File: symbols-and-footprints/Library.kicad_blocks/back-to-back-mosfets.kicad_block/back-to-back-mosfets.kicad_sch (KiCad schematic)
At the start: 6 parts

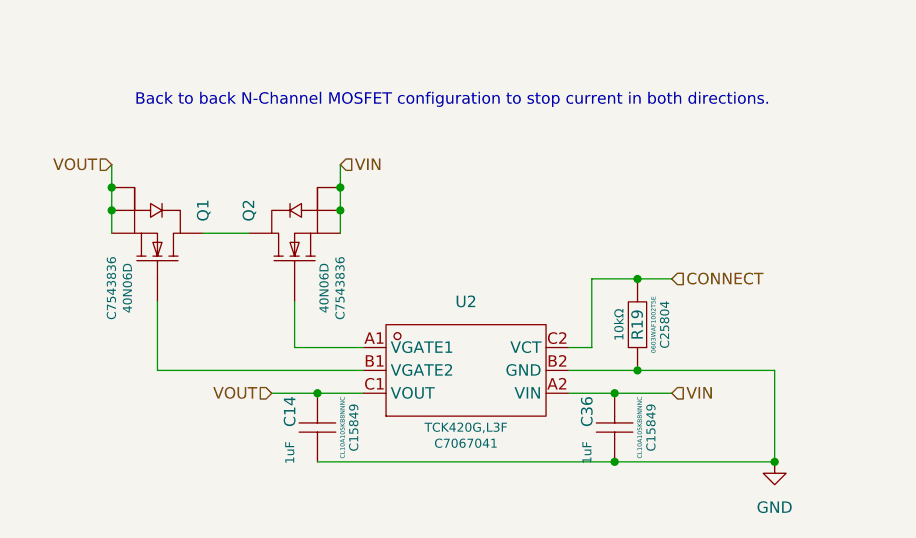
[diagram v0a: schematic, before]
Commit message: Almost complete new master circuit schematic.
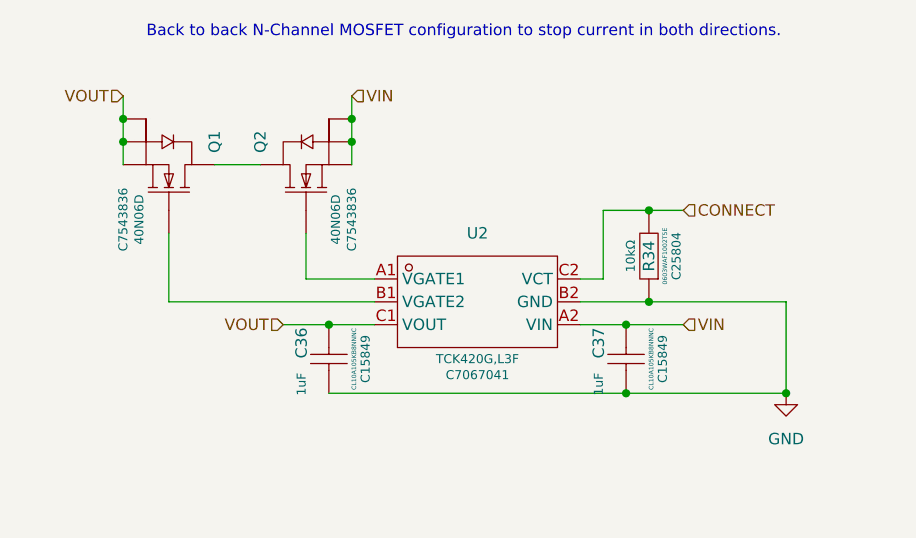
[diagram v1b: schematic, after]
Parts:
- removed C14: 1uF, Library:C0603, symbol Library:CL10A105KB8NNNC Capacitor 1uF
- removed R19: 10kΩ, Library:R0603, symbol Library:0603WAF1002T5E Resistor 10kΩ
- added C37: 1uF, Library:C0603, symbol Library:CL10A105KB8NNNC Capacitor 1uF
- added R34: 10kΩ, Library:R0603, symbol Library:0603WAF1002T5E Resistor 10kΩ
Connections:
- net CONNECT: now also R34.2
- net GND: now also C37.1, R34.1
- net VIN: now also C37.2; no longer C36.2
- net VOUT: now also C36.2
